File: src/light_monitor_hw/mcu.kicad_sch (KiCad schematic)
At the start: 8 parts, among them J2 Conn_01x02, J3 Conn_02x04_Odd_Even, SW2 NRST, U1 STM32L433VCTx, U2 FM24CL04B-GTR, Y1 Crystal_GND24

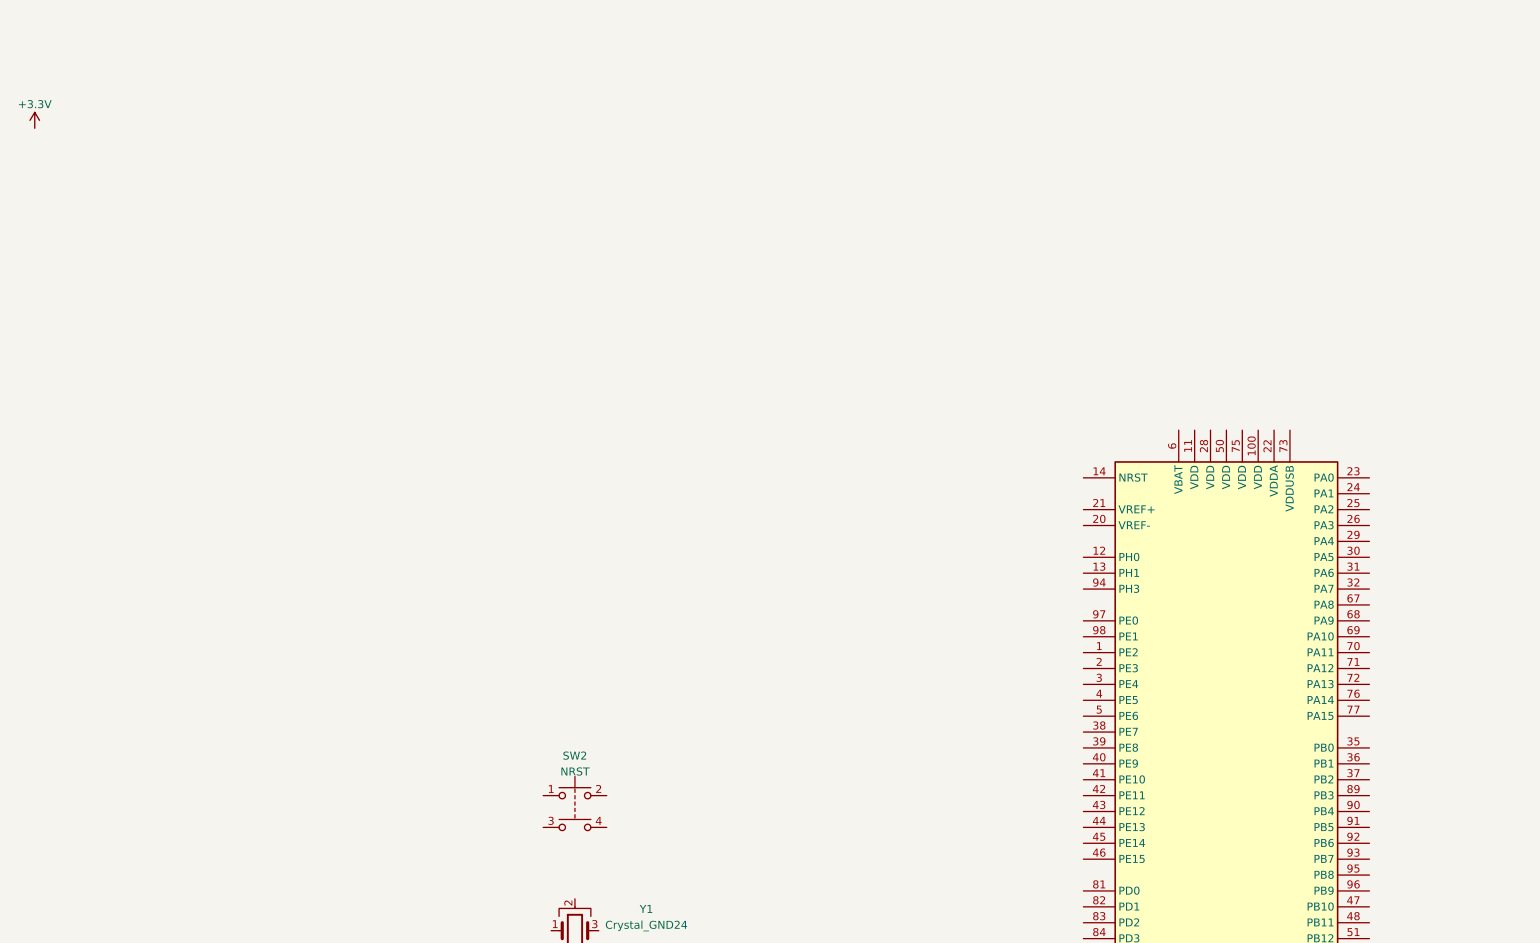
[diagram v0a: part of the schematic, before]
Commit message: [hw][fw] adding reset & boot to mcu, starting power decoupling
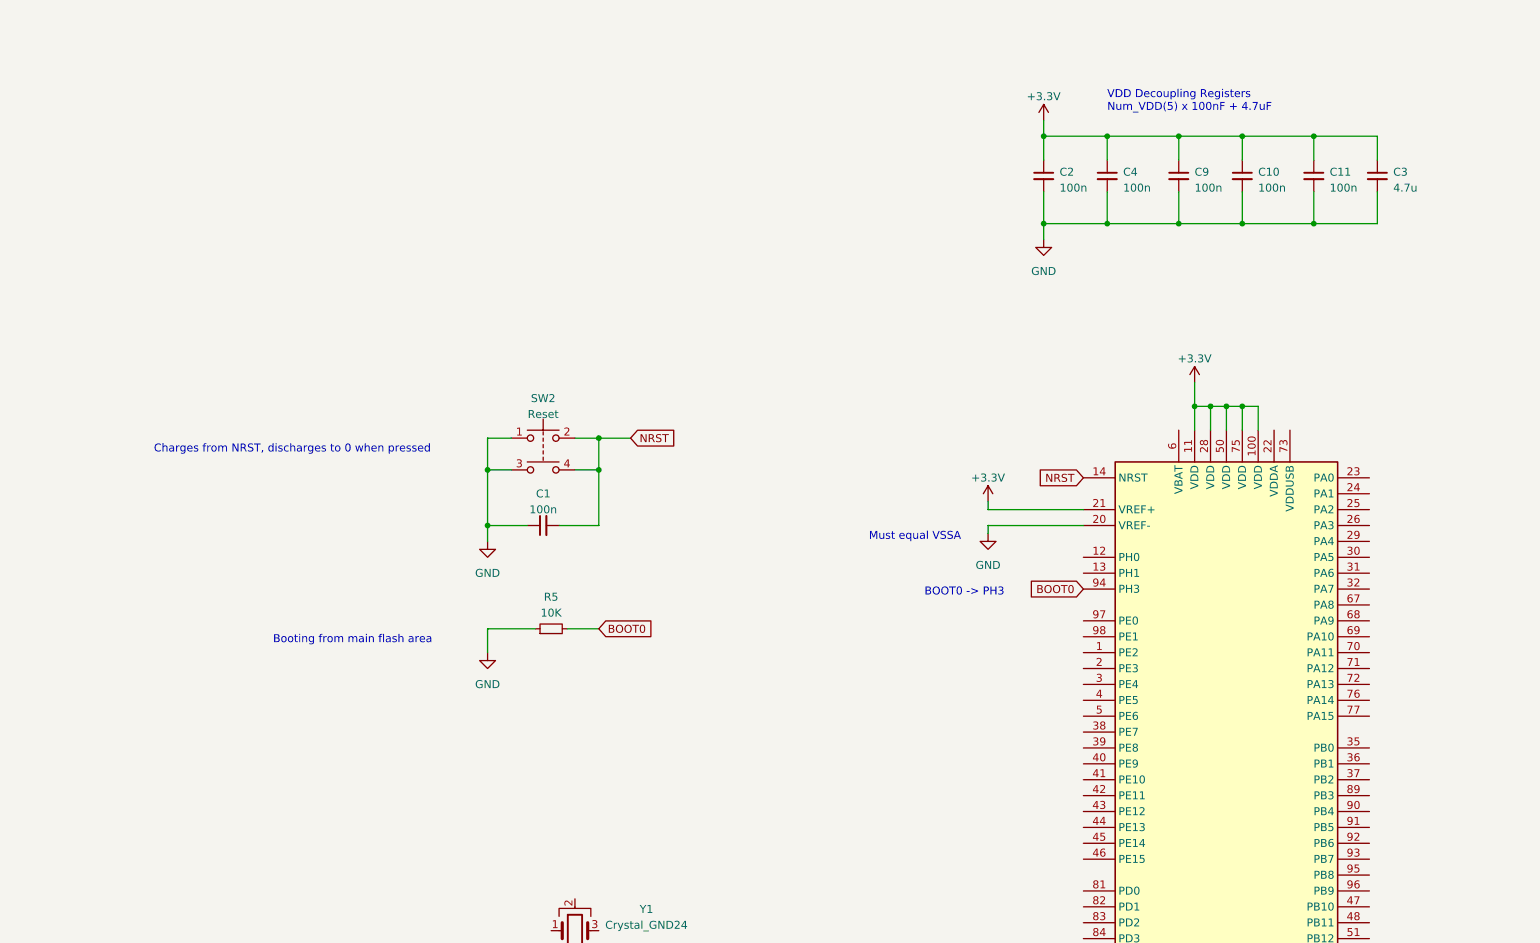
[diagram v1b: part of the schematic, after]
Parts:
- added C1, C10, C11, C2, C4, C9: 100n, symbol Device:C_Small
- added C3: 4.7u, symbol Device:C_Small
- added R5: 10K, symbol Device:R_Small
- SW2: value NRST -> Reset
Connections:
- net +3.3V: now also U1.100 (VDD), U1.11 (VDD), U1.21 (VREF+), U1.28 (VDD), U1.50 (VDD), U1.75 (VDD), C10.1, C11.1, C2.1, C3.1, C4.1, C9.1
- net GND: now also SW2.1, SW2.3, U1.20 (VREF-), C1.1, C10.2, C11.2, C2.2, C3.2, C4.2, C9.2, R5.1
- net NRST: now reaches U1.14 (NRST)
- net NRST: now also SW2.2, SW2.4, C1.2
- net BOOT0: now reaches U1.94 (PH3)
- net BOOT0: now also R5.2
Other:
- note added: "BOOT0 -> PH3"
- note added: "Booting from main flash area"
- note added: "Charges from NRST, discharges to 0 when pressed"
- note added: "Must equal VSSA"
- note added: "VDD Decoupling Registers Num_VDD(5) x 100nF + 4.7uF"
- moved on the sheet: SW2

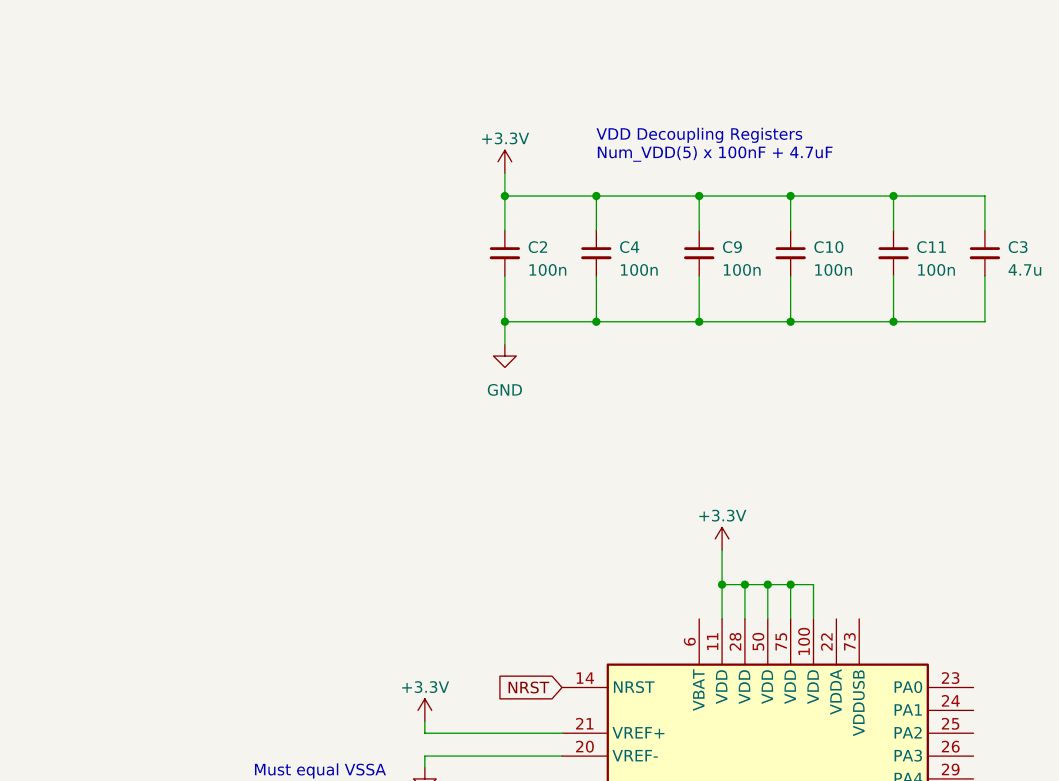
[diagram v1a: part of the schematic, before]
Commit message: [hw] added battery decoupling capacitors
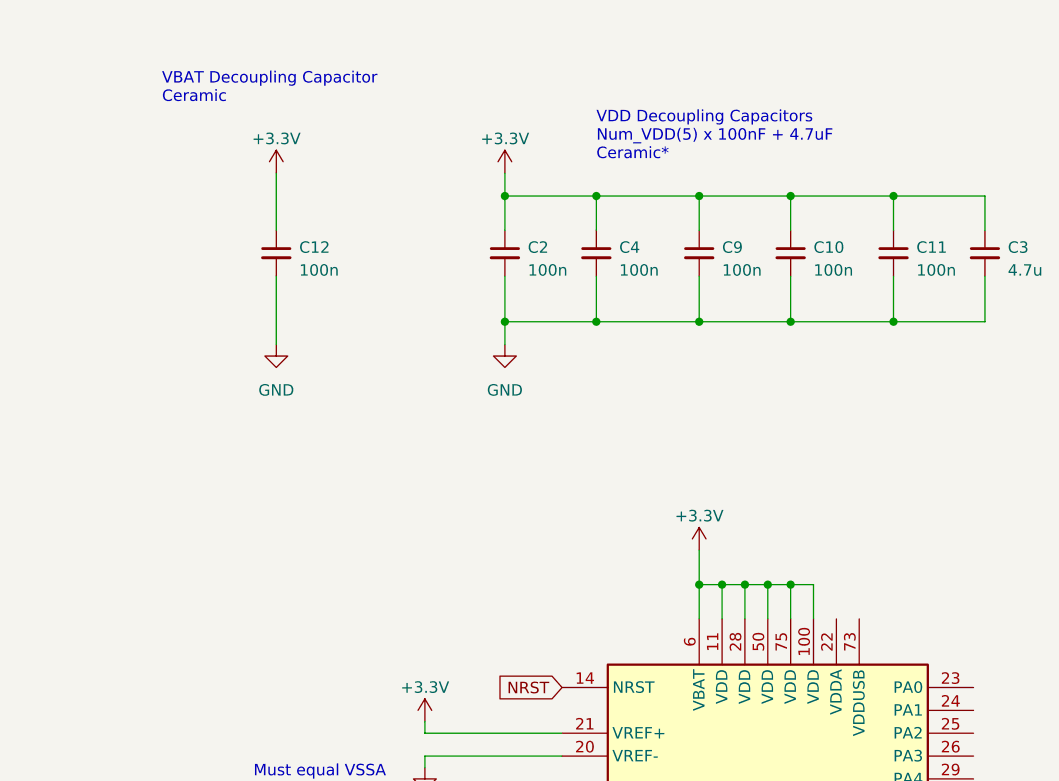
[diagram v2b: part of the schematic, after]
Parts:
- added C12: 100n, symbol Device:C_Small
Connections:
- net +3.3V: now also U1.6 (VBAT), C12.1
- net GND: now also C12.2
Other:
- note added: "VBAT Decoupling Capacitor Ceramic"
- note added: "VDD Decoupling Capacitors Num_VDD(5) x 100nF + 4.7uF Ceramic*"
- note removed: "VDD Decoupling Registers Num_VDD(5) x 100nF + 4.7uF"
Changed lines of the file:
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@@
   (junction (at 203.2 35.56) (diameter 0) (color 0 0 0 0)
   )
+  (junction (at 214.63 78.74) (diameter 0) (color 0 0 0 0)
+  )
   (junction (at 214.63 49.53) (diameter 0) (color 0 0 0 0)
   )
@@
     (stroke (width 0) (type default))
   )
+  (wire (pts (xy 167.64 33.02) (xy 167.64 39.37))
+    (stroke (width 0) (type default))
+  )
   (wire (pts (xy 214.63 49.53) (xy 203.2 49.53))
     (stroke (width 0) (type default))
@@
     (stroke (width 0) (type default))
   )
+  (wire (pts (xy 214.63 78.74) (xy 217.17 78.74))
+    (stroke (width 0) (type default))
+  )
   (wire (pts (xy 203.2 35.56) (xy 193.04 35.56))
     (stroke (width 0) (type default))
@@
     (stroke (width 0) (type default))
   )
+  (wire (pts (xy 167.64 44.45) (xy 167.64 52.07))
+    (stroke (width 0) (type default))
+  )
   (wire (pts (xy 193.04 39.37) (xy 193.04 35.56))
     (stroke (width 0) (type default))
@@
     (stroke (width 0) (type default))
   )
+  (wire (pts (xy 214.63 78.74) (xy 214.63 82.55))
+    (stroke (width 0) (type default))
+  )
   (wire (pts (xy 246.38 44.45) (xy 246.38 49.53))
     (stroke (width 0) (type default))
@@
     (stroke (width 0) (type default))
   )
-  (wire (pts (xy 217.17 74.93) (xy 217.17 78.74))
-    (stroke (width 0) (type default))
-  )
   (wire (pts (xy 104.14 97.79) (xy 104.14 88.9))
     (stroke (width 0) (type default))
@@
   )
   (wire (pts (xy 236.22 35.56) (xy 224.79 35.56))
+    (stroke (width 0) (type default))
+  )
+  (wire (pts (xy 214.63 74.93) (xy 214.63 78.74))
     (stroke (width 0) (type default))
   )
@@
     (effects (font (size 1.27 1.27)) (justify left bottom))
   )
-  (text "VDD Decoupling Registers\nNum_VDD(5) x 100nF + 4.7uF"
+  (text "VDD Decoupling Capacitors\nNum_VDD(5) x 100nF + 4.7uF\nCeramic*"
     (at 203.2 31.75 0)
     (effects (font (size 1.27 1.27)) (justify left bottom))
   )
   (text "Serial Wire Debugger" (at 308.61 127 0)
+    (effects (font (size 1.27 1.27)) (justify left bottom))
+  )
+  (text "VBAT Decoupling Capacitor\nCeramic" (at 154.94 25.4 0)
     (effects (font (size 1.27 1.27)) (justify left bottom))
   )
@@
     )
   )
+  (symbol (lib_id "Device:C_Small") (at 167.64 41.91 0) (unit 1)
+    (in_bom yes) (on_board yes) (dnp no) (fields_autoplaced)
+    (property "Reference" "C12" (at 170.18 41.2813 0)
+      (effects (font (size 1.27 1.27)) (justify left))
+    )
+    (property "Value" "100n" (at 170.18 43.8213 0)
+      (effects (font (size 1.27 1.27)) (justify left))
+    )
+    (property "Footprint" "" (at 167.64 41.91 0)
+      (effects (font (size 1.27 1.27)) hide)
+    )
+    (property "Datasheet" "~" (at 167.64 41.91 0)
+      (effects (font (size 1.27 1.27)) hide)
+    )
+    (pin "1")
+    (pin "2")
+    (instances
+      (project "light_monitor_hw"
+        (path "/f2c5757f-e0e3-42ec-a3b9-27ce976e3a0f/4ae58507-ad12-4333-aba2-89db72063e7d"
+          (reference "C12") (unit 1)
+        )
+      )
+    )
+  )
   (symbol (lib_id "SamacSys_Parts:FM24CL04B-GTR") (at 313.69 191.77 0) (unit 1)
     (in_bom yes) (on_board yes) (dnp no) (fields_autoplaced)
@@
     )
   )
+  (symbol (lib_id "power:GND") (at 167.64 52.07 0) (unit 1)
+    (in_bom yes) (on_board yes) (dnp no) (fields_autoplaced)
+    (property "Reference" "#PWR011" (at 167.64 58.42 0)
+      (effects (font (size 1.27 1.27)) hide)
+    )
+    (property "Value" "GND" (at 167.64 57.15 0)
+      (effects (font (size 1.27 1.27)))
+    )
+    (property "Footprint" "" (at 167.64 52.07 0)
+      (effects (font (size 1.27 1.27)) hide)
+    )
+    (property "Datasheet" "" (at 167.64 52.07 0)
+      (effects (font (size 1.27 1.27)) hide)
+    )
+    (pin "1")
+    (instances
+      (project "light_monitor_hw"
+        (path "/f2c5757f-e0e3-42ec-a3b9-27ce976e3a0f/4ae58507-ad12-4333-aba2-89db72063e7d"
+          (reference "#PWR011") (unit 1)
+        )
+      )
+    )
+  )
   (symbol (lib_id "Switch:SW_Push_Dual") (at 113.03 83.82 0) (unit 1)
     (in_bom yes) (on_board yes) (dnp no) (fields_autoplaced)
@@
     )
   )
-  (symbol (lib_id "power:+3.3V") (at 217.17 74.93 0) (unit 1)
-    (in_bom yes) (on_board yes) (dnp no) (fields_autoplaced)
-    (property "Reference" "#PWR09" (at 217.17 78.74 0)
-      (effects (font (size 1.27 1.27)) hide)
-    )
-    (property "Value" "+3.3V" (at 217.17 71.12 0)
-      (effects (font (size 1.27 1.27)))
-    )
-    (property "Footprint" "" (at 217.17 74.93 0)
-      (effects (font (size 1.27 1.27)) hide)
-    )
-    (property "Datasheet" "" (at 217.17 74.93 0)
+  (symbol (lib_id "power:+3.3V") (at 214.63 74.93 0) (unit 1)
+    (in_bom yes) (on_board yes) (dnp no) (fields_autoplaced)
+    (property "Reference" "#PWR09" (at 214.63 78.74 0)
+      (effects (font (size 1.27 1.27)) hide)
+    )
+    (property "Value" "+3.3V" (at 214.63 71.12 0)
+      (effects (font (size 1.27 1.27)))
+    )
+    (property "Footprint" "" (at 214.63 74.93 0)
+      (effects (font (size 1.27 1.27)) hide)
+    )
+    (property "Datasheet" "" (at 214.63 74.93 0)
       (effects (font (size 1.27 1.27)) hide)
     )
@@
         )
       )
+    )
+  )
+  (symbol (lib_id "power:+3.3V") (at 167.64 33.02 0) (unit 1)
+    (in_bom yes) (on_board yes) (dnp no) (fields_autoplaced)
+    (property "Reference" "#PWR010" (at 167.64 36.83 0)
+      (effects (font (size 1.27 1.27)) hide)
+    )
+    (property "Value" "+3.3V" (at 167.64 29.21 0)
+      (effects (font (size 1.27 1.27)))
+    )
+    (property "Footprint" "" (at 167.64 33.02 0)
+      (effects (font (size 1.27 1.27)) hide)
+    )
+    (property "Datasheet" "" (at 167.64 33.02 0)
+      (effects (font (size 1.27 1.27)) hide)
+    )
+    (pin "1")
+    (instances
+      (project "light_monitor_hw"
+        (path "/f2c5757f-e0e3-42ec-a3b9-27ce976e3a0f/4ae58507-ad12-4333-aba2-89db72063e7d"
+          (reference "#PWR010") (unit 1)
+        )
+      )
